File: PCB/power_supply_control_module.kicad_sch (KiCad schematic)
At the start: 14 parts, among them J1 Conn_01x04, J2 Conn_01x04, J3 Conn_02x03_Odd_Even, SW1 SW_Push, SW2 SW_Push, SW3 RotaryEncoder, SW4 RotaryEncoder, U1 ATmega328P-A, U2 MCP4251-xxxx-SL, Y1 Crystal

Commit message: schematic and board WIP
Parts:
- added C1: 100nF, Capacitor_SMD:C_1206_3216Metric_Pad1.33x1.80mm_HandSolder, symbol Device:C_Small
- added C2: 1uF, Capacitor_SMD:C_1206_3216Metric_Pad1.33x1.80mm_HandSolder, symbol Device:C_Small
- added C3: 10uF, Capacitor_SMD:C_1206_3216Metric_Pad1.33x1.80mm_HandSolder, symbol Device:C_Small
- added H1, H2: MountingHole, MountingHole:MountingHole_3.2mm_M3_ISO7380, symbol Mechanical:MountingHole
- added R1: 10K, Resistor_SMD:R_1206_3216Metric_Pad1.30x1.75mm_HandSolder, symbol Device:R
- added R2, R3, R4, R5: 1K, Resistor_SMD:R_1206_3216Metric_Pad1.30x1.75mm_HandSolder, symbol Device:R
- C4: renamed from C2; value C_Small -> 22pF; footprint (none) -> Capacitor_SMD:C_1206_3216Metric_Pad1.33x1.80mm_HandSolder
- C5: renamed from C1; value C_Small -> 22pF; footprint (none) -> Capacitor_SMD:C_1206_3216Metric_Pad1.33x1.80mm_HandSolder
- D1: renamed from D2; value LED -> Voltage; footprint (none) -> LED_SMD:LED_0603_1608Metric_Pad1.05x0.95mm_HandSolder
- D2: renamed from D1; value LED -> Current; footprint (none) -> LED_SMD:LED_0603_1608Metric_Pad1.05x0.95mm_HandSolder
- J1: renamed from J3; value Conn_02x03_Odd_Even -> ICSP; footprint (none) -> Connector_PinHeader_2.54mm:PinHeader_2x03_P2.54mm_Vertical
- J2: value Conn_01x04 -> PS_POT; footprint (none) -> Connector_JST:JST_XH_B4B-XH-A_1x04_P2.50mm_Vertical
- J3: renamed from J1; value Conn_01x04 -> PWR+UART; footprint (none) -> Connector_PinHeader_2.54mm:PinHeader_1x04_P2.54mm_Vertical; Field5 (none) -> USB A conn
- SW1: value SW_Push -> Voltage; footprint (none) -> Button_Switch_THT:SW_TH_Tactile_Omron_B3F-107x
- SW2: value SW_Push -> Current; footprint (none) -> Button_Switch_THT:SW_TH_Tactile_Omron_B3F-107x
- SW3: value RotaryEncoder -> Voltage
- SW4: value RotaryEncoder -> Current
- U2: value MCP4251-xxxx-SL -> MCP4251-103E-SL
- Y1: footprint (none) -> Crystal:Crystal_HC49-4H_Vertical
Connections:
- net GNDD: now also C4.2, C5.2, D1.1 (K), D2.1 (K), J1.6 (Pin_6), J3.4 (Pin_4), SW1.2, SW2.2, SW3.C, SW4.C, U1.21 (GND), U1.3 (GND), U1.5 (GND), U2.4 (VSS), C1.2, C2.2, C3.2
- net VCC: now also J1.2 (Pin_2), J3.1 (Pin_1), U1.18 (AVCC), U1.4 (VCC), U1.6 (VCC), U2.14 (VDD), C1.1, C2.1, C3.1, R1.2
- net ENC_A_A: now reaches SW4.A
- net ENC_A_A: now also U1.10 (PD6)
- net ENC_A_B: now reaches SW4.B
- net ENC_A_B: now also U1.11 (PD7)
- net SW_V: now reaches SW1.1
- net SW_V: now also U1.32 (PD2)
- net at C4.1: now also U1.8 (XTAL2/PB7), Y1.1
- net _POT_A: now reaches J2.1 (Pin_1)
- net _POT_A: now also U2.9 (P0W)
- net _POT_V: now reaches J2.2 (Pin_2)
- net _POT_V: now also U2.6 (P1W)
- net _GND: now reaches J2.3 (Pin_3)
- net _GND: now also U2.10 (P0B), U2.5 (P1B)
- net _VCC: now reaches J2.4 (Pin_4)
- net _VCC: now also U2.7 (P1A), U2.8 (P0A)
- net at D2.2 (A): now also R3.1
- net MISO: now reaches J1.1 (Pin_1)
- net MISO: now also U1.16 (PB4), U2.13 (SDO)
- net SCK: now reaches J1.3 (Pin_3)
- net SCK: now also U1.17 (PB5), U2.2 (SCK)
- net MOSI: now reaches J1.4 (Pin_4)
- net MOSI: now also U1.15 (PB3), U2.3 (SDI)
- net RST: now reaches J1.5 (Pin_5)
- net RST: now also U1.29 (~{RESET}/PC6)
- net at J3.2 (Pin_2): now also R4.2
- net at J3.3 (Pin_3): now also R5.1
- net at D1.2 (A): now also R2.2
- net ENC_V_A: now reaches SW3.A
- net ENC_V_A: now also U1.2 (PD4)
- net ENC_V_B: now reaches SW3.B
- net ENC_V_B: now also U1.9 (PD5)
- net SW_A: now reaches SW2.1
- net SW_A: now also U1.1 (PD3)
- net ~{MCP_CS}: now reaches U1.14 (PB2)
- net ~{MCP_CS}: now also U2.1 (~{CS}), R1.1
- net LED_V: now reaches U1.25 (PC2)
- net LED_V: now also R2.1
- net LED_A: now reaches U1.26 (PC3)
- net LED_A: now also R3.2
- net RXD0: now reaches U1.30 (PD0)
- net RXD0: now also R4.1
- net TXD0: now reaches U1.31 (PD1)
- net TXD0: now also R5.2
- net at U1.7 (XTAL1/PB6): now also C5.1, Y1.2
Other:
- note added: "Interconnection and pinout based on original circuit."
- note added: "Pull-up to disconnect SPI on boot-up"
- note added: "Resistors for MCU protection, USB should not be used for charging!"
- note added: "TODO: Check MCP datasheet! TODO: FInd out what to do with AREF and ADC pins. TODO: Create SW! TODO: DRC"
- note added: "Using internal pull-ups."
- title: (none) -> Laboratory power supply control module
- moved on the sheet: C4, C5, D1, D2, J1, J2, J3, SW1, SW2, SW3, SW4, U1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

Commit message: second MCP added WIP
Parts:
- added R10, R11, R7, R8, R9: 10K, Resistor_SMD:R_1206_3216Metric_Pad1.30x1.75mm_HandSolder, symbol Device:R
- added R4: 2k, Resistor_SMD:R_1206_3216Metric_Pad1.30x1.75mm_HandSolder, symbol Device:R
- added U3: MCP4251-103E-SL, Package_SO:SOIC-14_3.9x8.7mm_P1.27mm, symbol Potentiometer_Digital:MCP4251-xxxx-SL
- renumbered R4 to R5, R5 to R6
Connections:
- net GNDD: now also U3.4 (VSS)
- net MISO: now also U3.13 (SDO)
- net MOSI: now also U3.3 (SDI)
- net SCK: now also U3.2 (SCK)
- net VCC: now also R7.2, U3.14 (VDD)
- net ~{MCP_CS2}: now reaches U1.13 (PB1)
- net ~{MCP_CS2}: now also R7.1, U3.1 (~{CS})
- net ENC_A_A renamed ENC_C_A
- net ENC_A_B renamed ENC_C_B
- net _GND renamed GND1
- net GND1: now also R10.1, R11.2
- net _POT_A renamed _POT_C
- removed net _VCC: J2.4 (Pin_4), U2.7 (P1A), U2.8 (P0A)
- net ~{MCP_CS} renamed ~{MCP_CS1}
- new net: R11.1, R8.1, U2.8 (P0A), U3.10 (P0B), U3.9 (P0W)
- new net: R10.2, R9.1, U2.7 (P1A), U3.5 (P1B), U3.6 (P1W)
- new net: R4.2, R9.2, U3.7 (P1A)
- new net VCC2: J2.4 (Pin_4), R4.1, R8.2, U3.8 (P0A)
- no-connect marks 0 -> 4
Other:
- note added: "R4=2k -> compensate for missing fine pot (1.5+0.5)"
- note added: "Using internal pull-ups. R=~3k"
- moved on the sheet: C1, C2, C3, C4, C5, D1, D2, J1, J2, J3, R1, R2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

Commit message: Schematic finished
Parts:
- added C4, C7: 100nF, Capacitor_SMD:C_1206_3216Metric_Pad1.33x1.80mm_HandSolder, symbol Device:C_Small
- renumbered C4 to C5, C5 to C6, J3 to J2, J2 to J3, R7 to R1, R11 to R10, R10 to R11, R8 to R2, R4 to R3, R2 to R4, R3 to R5, R9 to R6, R5 to R7, R6 to R8, R1 to R9, U3 to U1, U1 to U2, U2 to U3
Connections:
- net GNDD: now also C4.2, C7.2
- net VCC: now also C4.1, C7.1
- net GND1 renamed GND2
- net LED_A renamed LED_C
- net SW_A renamed SW_C
- no-connect marks 4 -> 12
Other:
- note added: "10k paraller R used to ensure R_{max}=5.5k"
- note added: "LEDs from arduino nano"
- note added: "NOTES: To disable second DPOT: > short-circuit R2, R6 > remove R10, R11 Interconnection of digital pots and pinout of PS_POT conn is based on original power supply circuit."
- note added: "R3=2k -> compensate for missing fine pot (1.5+0.5)"
- note removed: "Interconnection and pinout based on original circuit."
- note removed: "R4=2k -> compensate for missing fine pot (1.5+0.5)"
- note removed: "TODO: Check MCP datasheet! TODO: FInd out what to do with AREF and ADC pins. TODO: Create SW! TODO: DRC"
- company: (none) -> Design by: Martin Tavoda
- moved on the sheet: C1, C2, C3, C5, C6, D1, D2, H1, H2, J1, J2, J3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

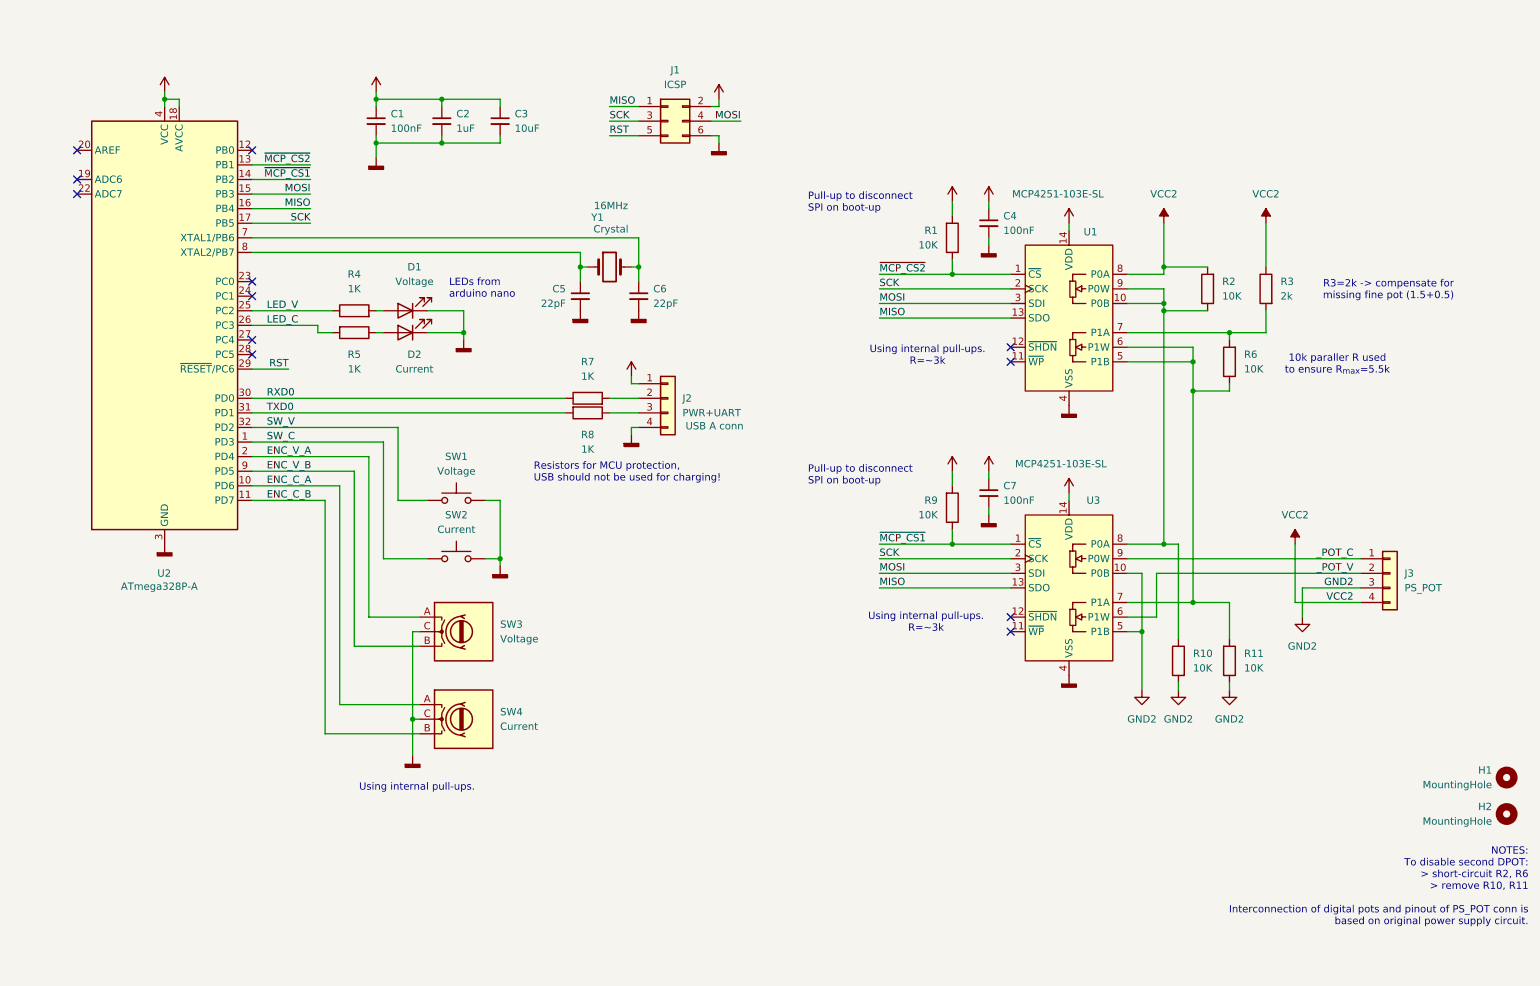
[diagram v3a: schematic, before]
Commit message: added USB PCB, before connecting the PCBs
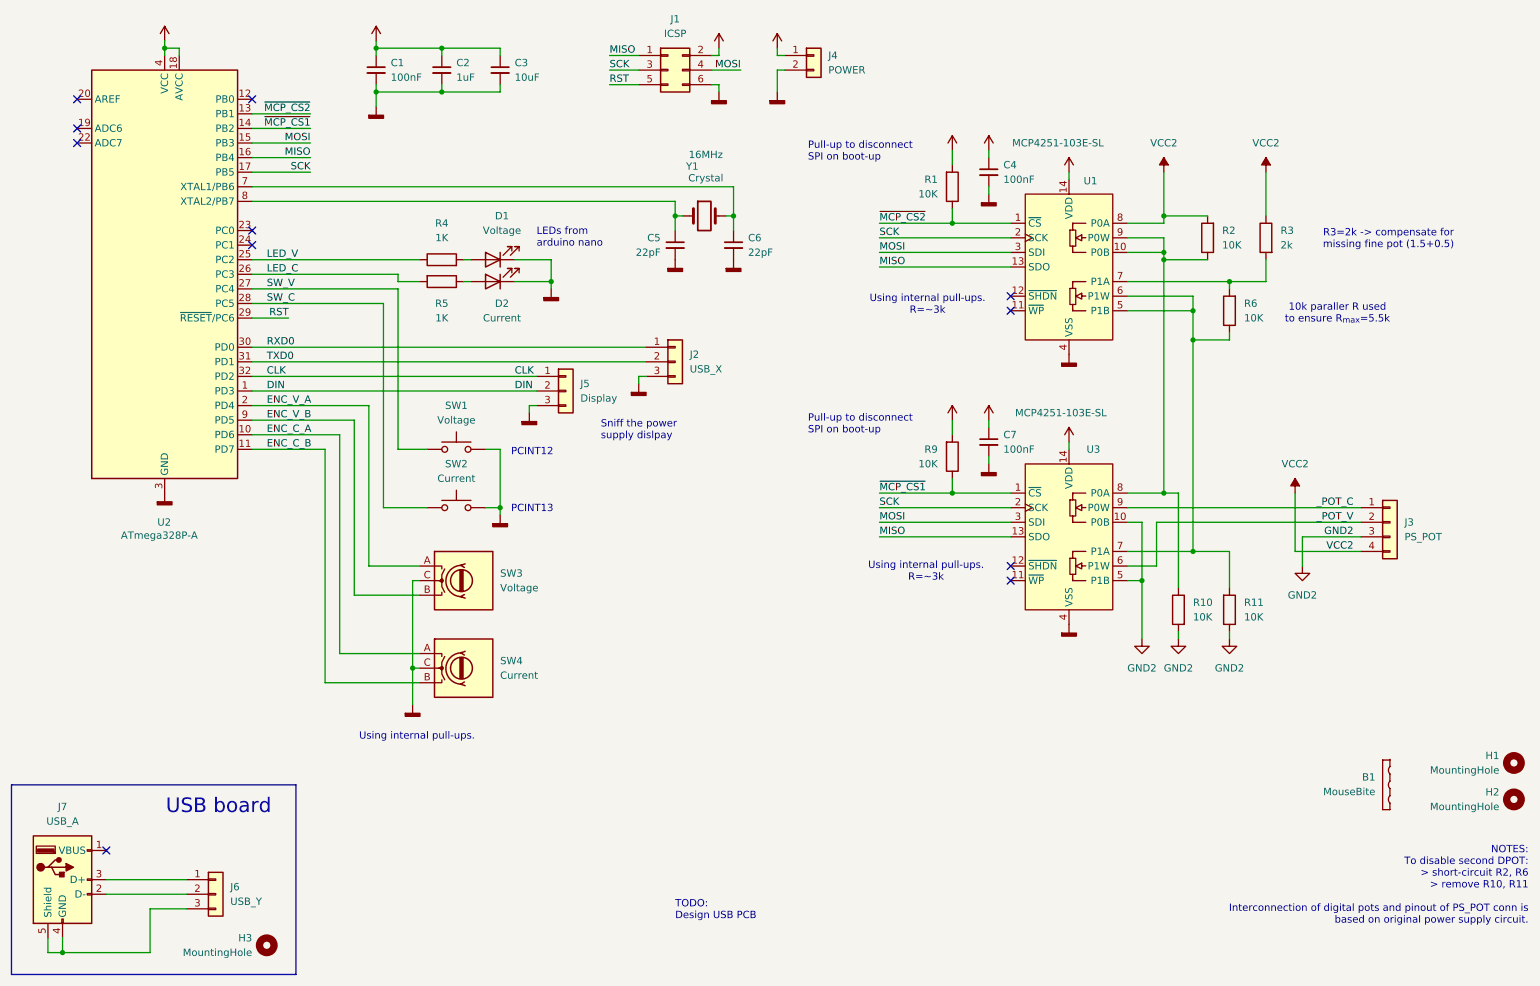
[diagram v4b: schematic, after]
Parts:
- removed J2: PWR+UART, Connector_PinHeader_2.54mm:PinHeader_1x04_P2.54mm_Vertical, symbol Connector_Generic:Conn_01x04
- removed R7, R8: 1K, Resistor_SMD:R_1206_3216Metric_Pad1.30x1.75mm_HandSolder, symbol Device:R
- added B1: MouseBite, lib:mouse-bite-2mm-slot, symbol Mechanical:MouseBite
- added H3: MountingHole, MountingHole:MountingHole_3.2mm_M3_ISO7380, symbol Mechanical:MountingHole
- added J2: USB_X, EDAC:SHDR3W50P0X200_1X3_800X470X640P, symbol Connector_Generic:Conn_01x03
- added J4: POWER, EDAC:140502415001, symbol Connector_Generic:Conn_01x02
- added J5: Display, EDAC:SHDR3W50P0X200_1X3_800X470X640P, symbol Connector_Generic:Conn_01x03
- added J6: USB_Y, Connector_PinHeader_2.00mm:PinHeader_1x03_P2.00mm_Vertical, symbol Connector_Generic:Conn_01x03
- added J7: USB_A, Connector_USB:USB_A_Molex_105057_Vertical, symbol Connector:USB_A
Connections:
- net GNDD: now also J2.3 (Pin_3), J4.2 (Pin_2), J5.3 (Pin_3)
- net RXD0: now also J2.1 (Pin_1)
- net SW_C: now also U2.28 (PC5); no longer U2.1 (PD3)
- net SW_V: now also U2.27 (PC4); no longer U2.32 (PD2)
- net TXD0: now also J2.2 (Pin_2)
- net VCC: now also J4.1 (Pin_1)
- new net: J6.2 (Pin_2), J7.2 (D-)
- new net: J6.1 (Pin_1), J7.3 (D+)
- new net: J6.3 (Pin_3), J7.4 (GND), J7.5 (Shield)
- new net CLK: J5.1 (Pin_1), U2.32 (PD2)
- new net DIN: J5.2 (Pin_2), U2.1 (PD3)
- no-connect marks 12 -> 11
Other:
- note added: "PCINT12"
- note added: "PCINT13"
- note added: "Sniff the power supply dislpay"
- note added: "TODO: Design USB PCB"
- note added: "USB board"
- note removed: "Resistors for MCU protection, USB should not be used for charging!"
- moved on the sheet: C1, C2, C3, C4, C5, C6, C7, D1, D2, H1, H2, J1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

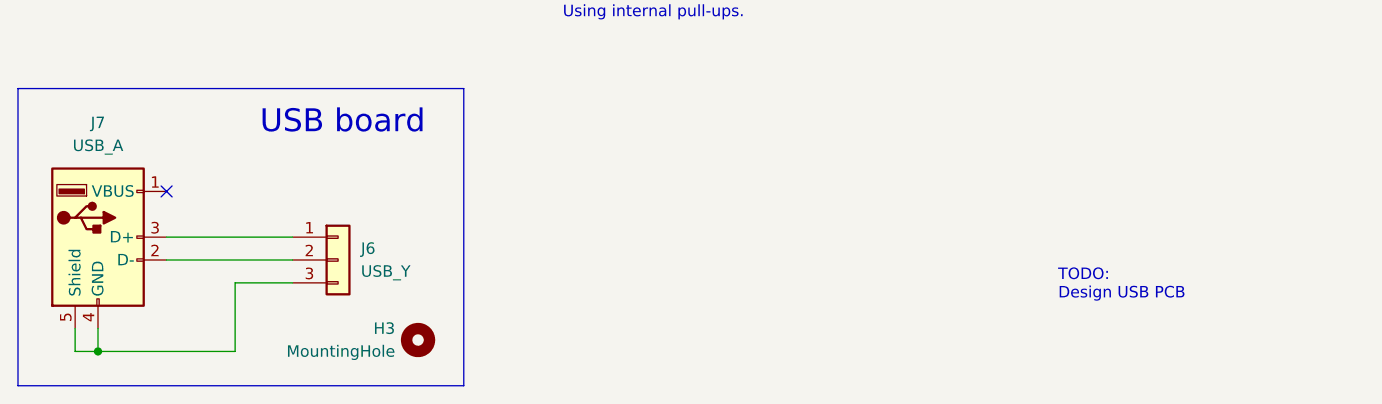
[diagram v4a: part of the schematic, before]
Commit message: USB PCB finished
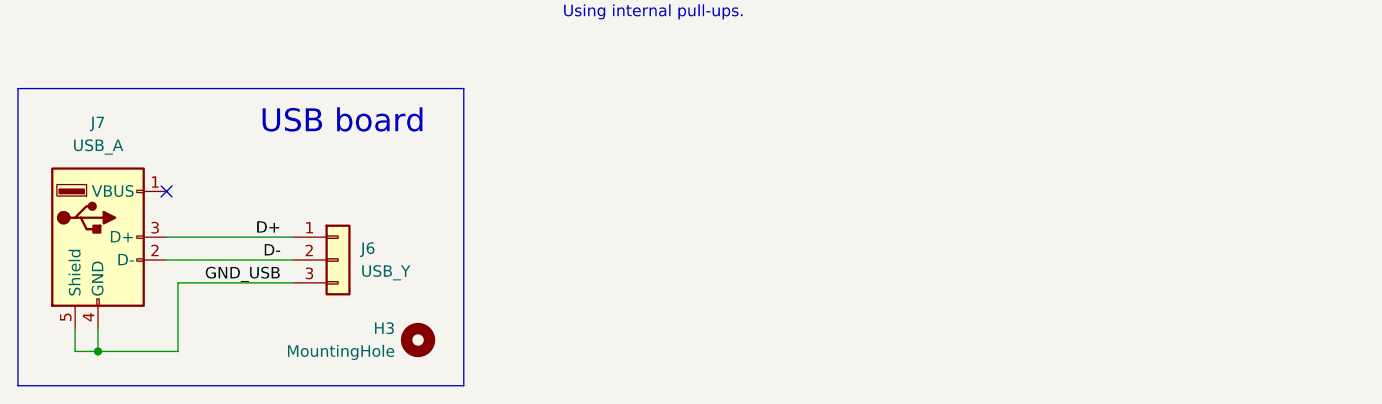
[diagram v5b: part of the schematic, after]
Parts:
- B1: footprint lib:mouse-bite-2mm-slot -> lib:mouse-bite-3mm-slot-jlcpcb
- J7: footprint Connector_USB:USB_A_Molex_105057_Vertical -> USB_A:USB_A_Molex_105057_Vertical
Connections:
- net D-: now reaches J6.2 (Pin_2), J7.2 (D-)
- net D+: now reaches J6.1 (Pin_1), J7.3 (D+)
- net GND_USB: now reaches J6.3 (Pin_3), J7.4 (GND), J7.5 (Shield)
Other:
- note removed: "TODO: Design USB PCB"
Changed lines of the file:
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@@
 		)
 	)
-	(text "TODO:\nDesign USB PCB"
-		(exclude_from_sim no)
-		(at 134.62 178.054 0)
-		(effects
-			(font
-				(size 1.27 1.27)
-				(color 255 0 3 1)
-			)
-			(justify left)
-		)
-	)
 	(text "PCINT13"
 		(exclude_from_sim no)
@@
 	(wire
 		(pts
-			(xy 43.18 177.8) (xy 43.18 185.42)
+			(xy 36.83 177.8) (xy 36.83 185.42)
 		)
 		(stroke
@@
 	(wire
 		(pts
-			(xy 43.18 185.42) (xy 27.94 185.42)
-		)
-		(stroke
-			(width 0)
-			(type default)
-		)
-	)
-	(wire
-		(pts
 			(xy 182.88 45.72) (xy 182.88 48.26)
 		)
@@
 	(wire
 		(pts
-			(xy 49.53 177.8) (xy 43.18 177.8)
+			(xy 36.83 177.8) (xy 49.53 177.8)
 		)
 		(stroke
@@
 	(wire
 		(pts
+			(xy 27.94 185.42) (xy 36.83 185.42)
+		)
+		(stroke
+			(width 0)
+			(type default)
+		)
+	)
+	(wire
+		(pts
 			(xy 35.56 175.26) (xy 49.53 175.26)
 		)
@@
 		)
 	)
+	(label "GND_USB"
+		(at 48.26 177.8 180)
+		(effects
+			(font
+				(size 1.27 1.27)
+			)
+			(justify right bottom)
+		)
+	)
 	(label "MISO"
 		(at 71.12 46.99 180)
@@
 		)
 	)
+	(label "D-"
+		(at 48.26 175.26 180)
+		(effects
+			(font
+				(size 1.27 1.27)
+			)
+			(justify right bottom)
+		)
+	)
 	(label "MOSI"
 		(at 170.18 110.49 0)
@@
 		)
 	)
+	(label "D+"
+		(at 48.26 172.72 180)
+		(effects
+			(font
+				(size 1.27 1.27)
+			)
+			(justify right bottom)
+		)
+	)
 	(label "_POT_V"
 		(at 252.73 110.49 180)
@@
 			)
 		)
-		(property "Footprint" "lib:mouse-bite-2mm-slot"
+		(property "Footprint" "lib:mouse-bite-3mm-slot-jlcpcb"
 			(at 257.81 156.21 0)
 			(effects
@@
 			)
 		)
-		(property "Footprint" "Connector_USB:USB_A_Molex_105057_Vertical"
+		(property "Footprint" "USB_A:USB_A_Molex_105057_Vertical"
 			(at 31.75 173.99 0)
 			(effects

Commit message: routing finished
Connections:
- net ~{MCP_CS1}: now also U2.13 (PB1); no longer U2.14 (PB2)
- net ~{MCP_CS2}: now also U2.14 (PB2); no longer U2.13 (PB1)
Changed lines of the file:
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@@
 	)
 	(label "~{MCP_CS2}"
-		(at 71.12 39.37 180)
+		(at 71.12 41.91 180)
 		(effects
 			(font
@@
 	)
 	(label "~{MCP_CS1}"
-		(at 71.12 41.91 180)
+		(at 71.12 39.37 180)
 		(effects
 			(font

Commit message: PCB finished, JLCPCB ordered
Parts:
- removed U2: ATmega328P-A, Package_QFP:TQFP-32_7x7mm_P0.8mm, symbol MCU_Microchip_ATmega:ATmega328P-A
- added U2: ATmega328PB-A, Package_QFP:TQFP-32_7x7mm_P0.8mm, symbol MCU_Microchip_ATmega:ATmega328PB-A
- J5: value Display -> DISP
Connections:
- net ENC_C_A: now also U2.10 (PD6)
- net ENC_C_B: now also U2.11 (PD7)
- net ENC_V_A: now also U2.2 (PD4)
- net ENC_V_B: now also U2.9 (PD5)
- net GNDD: now also SW3.MP, SW4.MP, U2.21 (GND), U2.5 (GND)
- net LED_C: now also U2.26 (PC3)
- net LED_V: now also U2.25 (PC2)
- net MISO: now also U2.16 (PB4)
- net MOSI: now also U2.15 (PB3)
- net RST: now also U2.29 (~{RESET}/PC6)
- net RXD0: now also U2.30 (PD0)
- net SCK: now also U2.17 (PB5)
- net SW_C: now also U2.28 (PC5)
- net SW_V: now also U2.27 (PC4)
- net TXD0: now also U2.31 (PD1)
- net VCC: now also U2.18 (AVCC), U2.4 (VCC)
- net ~{MCP_CS1}: now also U2.13 (PB1)
- net ~{MCP_CS2}: now also U2.14 (PB2)
- net at C5.1, Y1.1: now also U2.8 (XTAL2/PB7)
- net at C6.1, Y1.2: now also U2.7 (XTAL1/PB6)
- net CLK renamed DISP_CLK
- net DISP_CLK: now also U2.32 (PD2)
- net DIN renamed DISP_DIN
- net DISP_DIN: now also U2.1 (PD3)
- no-connect marks 11 -> 13
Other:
- note added: "16MHz"
- note removed: "PCINT12"
- note removed: "PCINT13"
- moved on the sheet: J4
